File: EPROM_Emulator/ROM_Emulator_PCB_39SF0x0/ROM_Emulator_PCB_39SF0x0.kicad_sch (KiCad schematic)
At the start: 10 parts, among them U1 SST39SF040, U2 Teensy4.1_Fewer_Pins, U3 74HC244, U4 74HC244, U5 74HC244, U7 74HC244

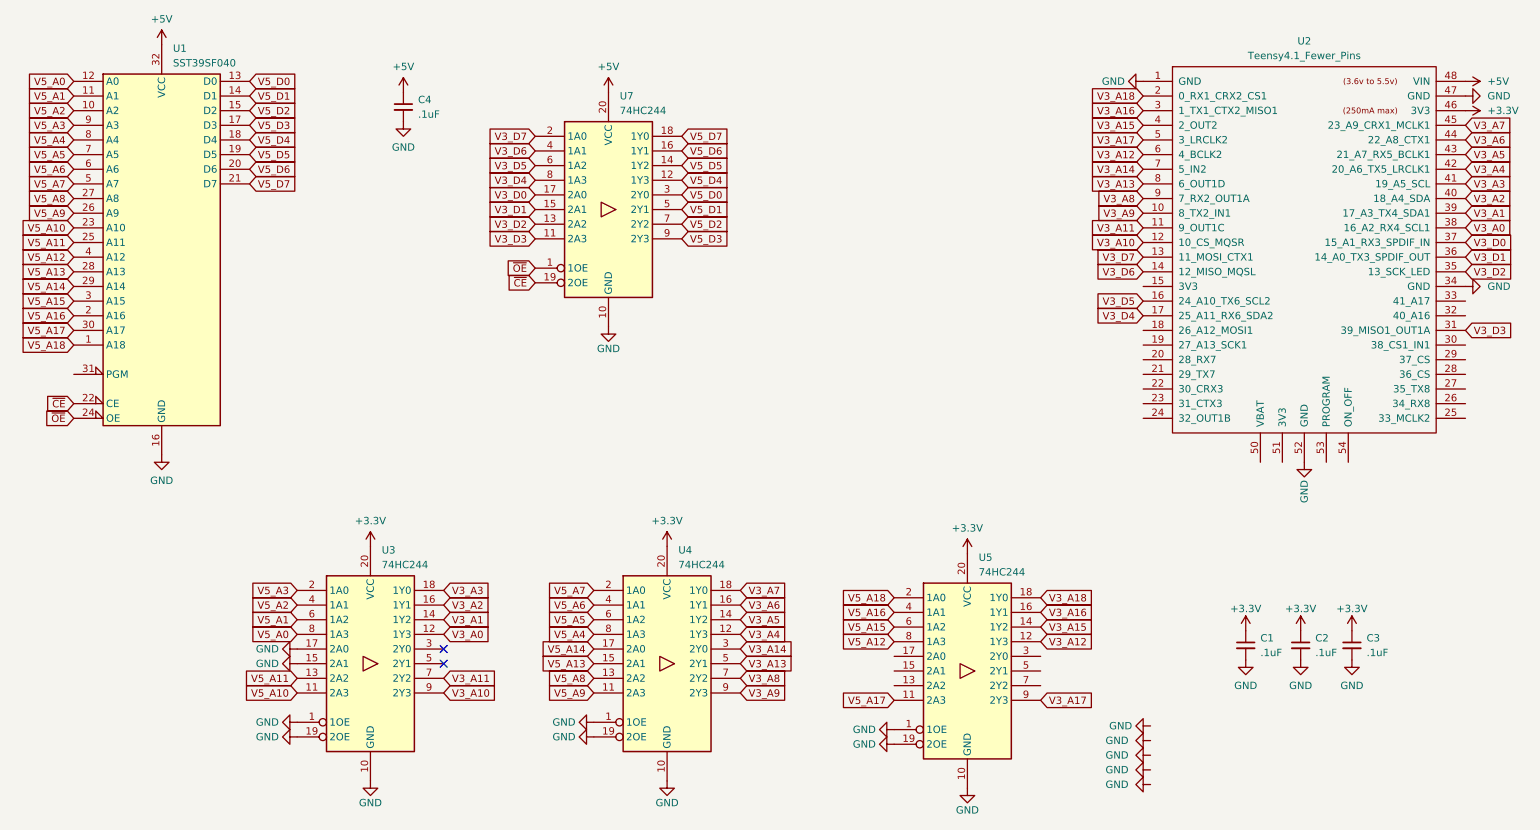
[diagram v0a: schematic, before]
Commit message: Bugfix: OR'd OE# and CE# together, used for both halves of data 244. Added some buttons. Freed up D13 for LED use.
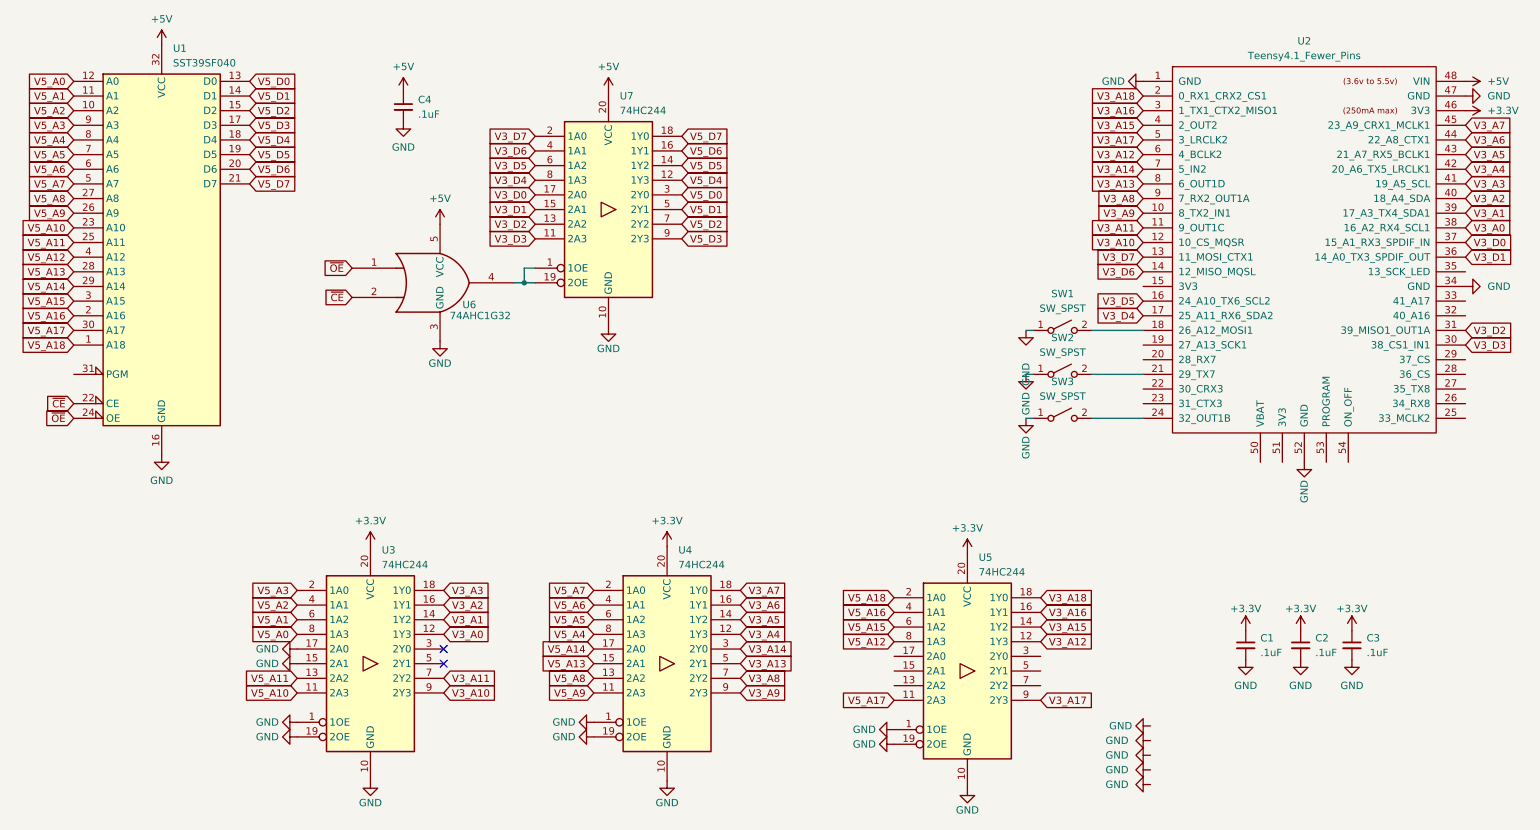
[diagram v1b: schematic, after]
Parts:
- added SW1, SW2, SW3: SW_SPST, Button_Switch_SMD:SW_SPST_B3U-1000P-B, symbol Switch:SW_SPST
- added U6: 74AHC1G32, Package_TO_SOT_SMD:SOT-353_SC-70-5, symbol 74xGxx:74AHC1G32
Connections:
- net +5V: now also U6.5 (VCC)
- net GND: now also SW1.1 (A), SW2.1 (A), SW3.1 (A), U6.3 (GND)
- net V3_D2: now also U2.31 (39_MISO1_OUT1A); no longer U2.35 (13_SCK_LED)
- net V3_D3: now also U2.30 (38_CS1_IN1); no longer U2.31 (39_MISO1_OUT1A)
- net ~{CE}: now also U6.2; no longer U7.19 (2OE)
- net ~{OE}: now also U6.1; no longer U7.1 (1OE)
- net at U2.18 (26_A12_MOSI1): now also SW1.2 (B)
- net at U2.21 (29_TX7): now also SW2.2 (B)
- net at U2.24 (32_OUT1B): now also SW3.2 (B)
- new net: U6.4, U7.1 (1OE), U7.19 (2OE)
